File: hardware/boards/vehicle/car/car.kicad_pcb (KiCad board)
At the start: 2 copper layers, 50 x 95 mm, 119 parts, among them J1 Conn_01x04_Socket, J10 Conn_02x03_Odd_Even, J2 Conn_01x05_Socket, J3 Conn_01x05_Socket, J4 Conn_01x05_Socket, J5 Conn_01x02_Socket, J6 SMA, J7 02x04, J8 Conn_01x04_Socket, J9 Conn_02x05_Odd_Even, M1 Motor_DC, M2 Motor_DC, Q1 FQP27P06, Q10 AO3400A, Q11 2N3904, Q12 2N3904, Q2 AO3400A, Q3 FQP27P06, Q4 AO3400A, Q5 2N3904, Q6 2N3904, Q7 FQP27P06, Q8 AO3400A, Q9 FQP27P06, SW1 SW_Push, U1 ATmega328P-A, U4 TPS54302, U5 AMS1117-3.3, U7 NRF24L01, U8 RFX2401C, Y1 8MHz, Y3 16MHz

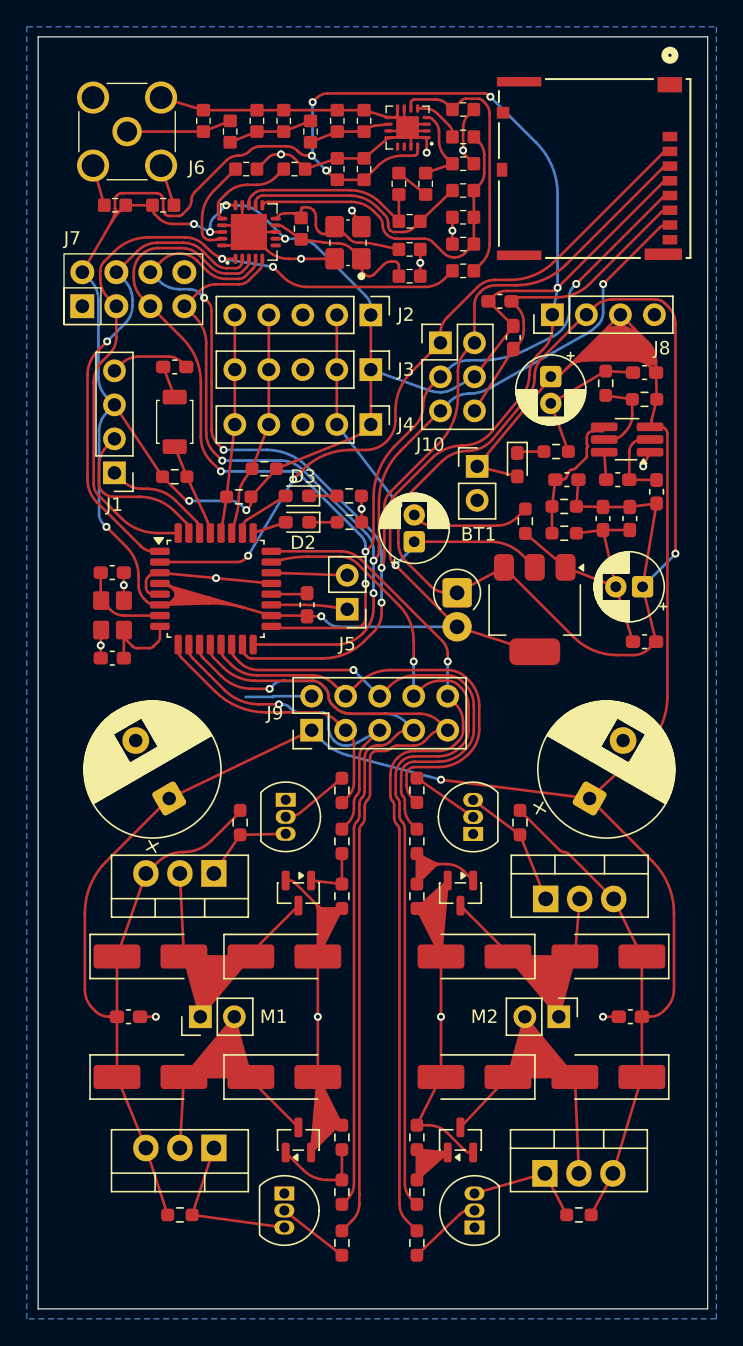
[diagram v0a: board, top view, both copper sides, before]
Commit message: edited inductor footprint for car and export gerber for lidar
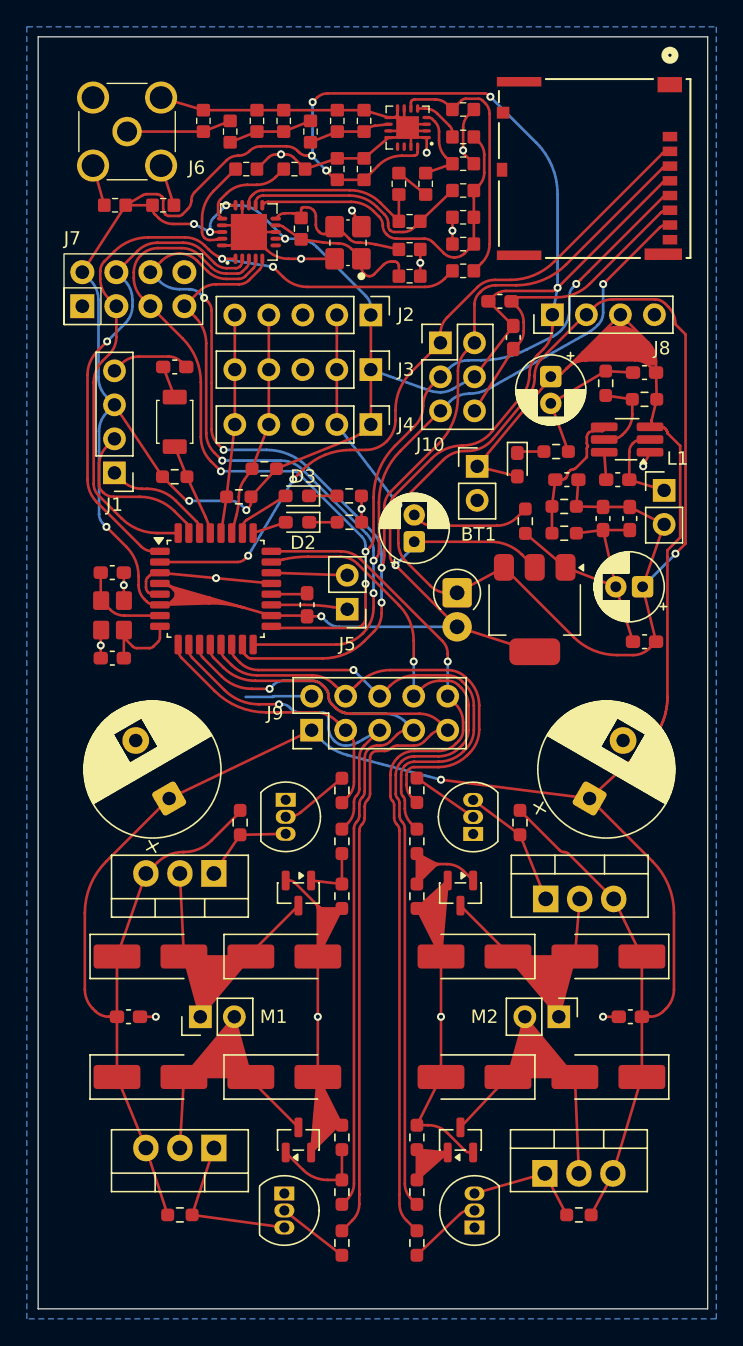
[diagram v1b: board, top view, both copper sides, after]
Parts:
- L1: footprint Inductor_SMD:L_0603_1608Metric_Pad1.05x0.95mm_HandSolder -> Connector_PinHeader_2.54mm:PinHeader_1x02_P2.54mm_Vertical
- moved L1 0.57 mm to (171.1, 88.1), turned to 0 degrees
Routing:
- net 3V3: track 274.9 -> 271.7 mm
- net 12V: track 210.8 -> 211.6 mm
- net Net-(U4-SW): track 6.17 -> 6.86 mm
